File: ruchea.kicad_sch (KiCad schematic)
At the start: 14 parts, among them J10 Conn_01x04, J11 Conn_01x04, J12 Conn_01x04, J14 Conn_01x03, J2 Conn_01x04, J3 Conn_01x03, J4 Conn_01x04, J5 Conn_01x04, J6 Conn_01x02, J7 Conn_01x02, J8 Conn_01x03, J9 Conn_01x03

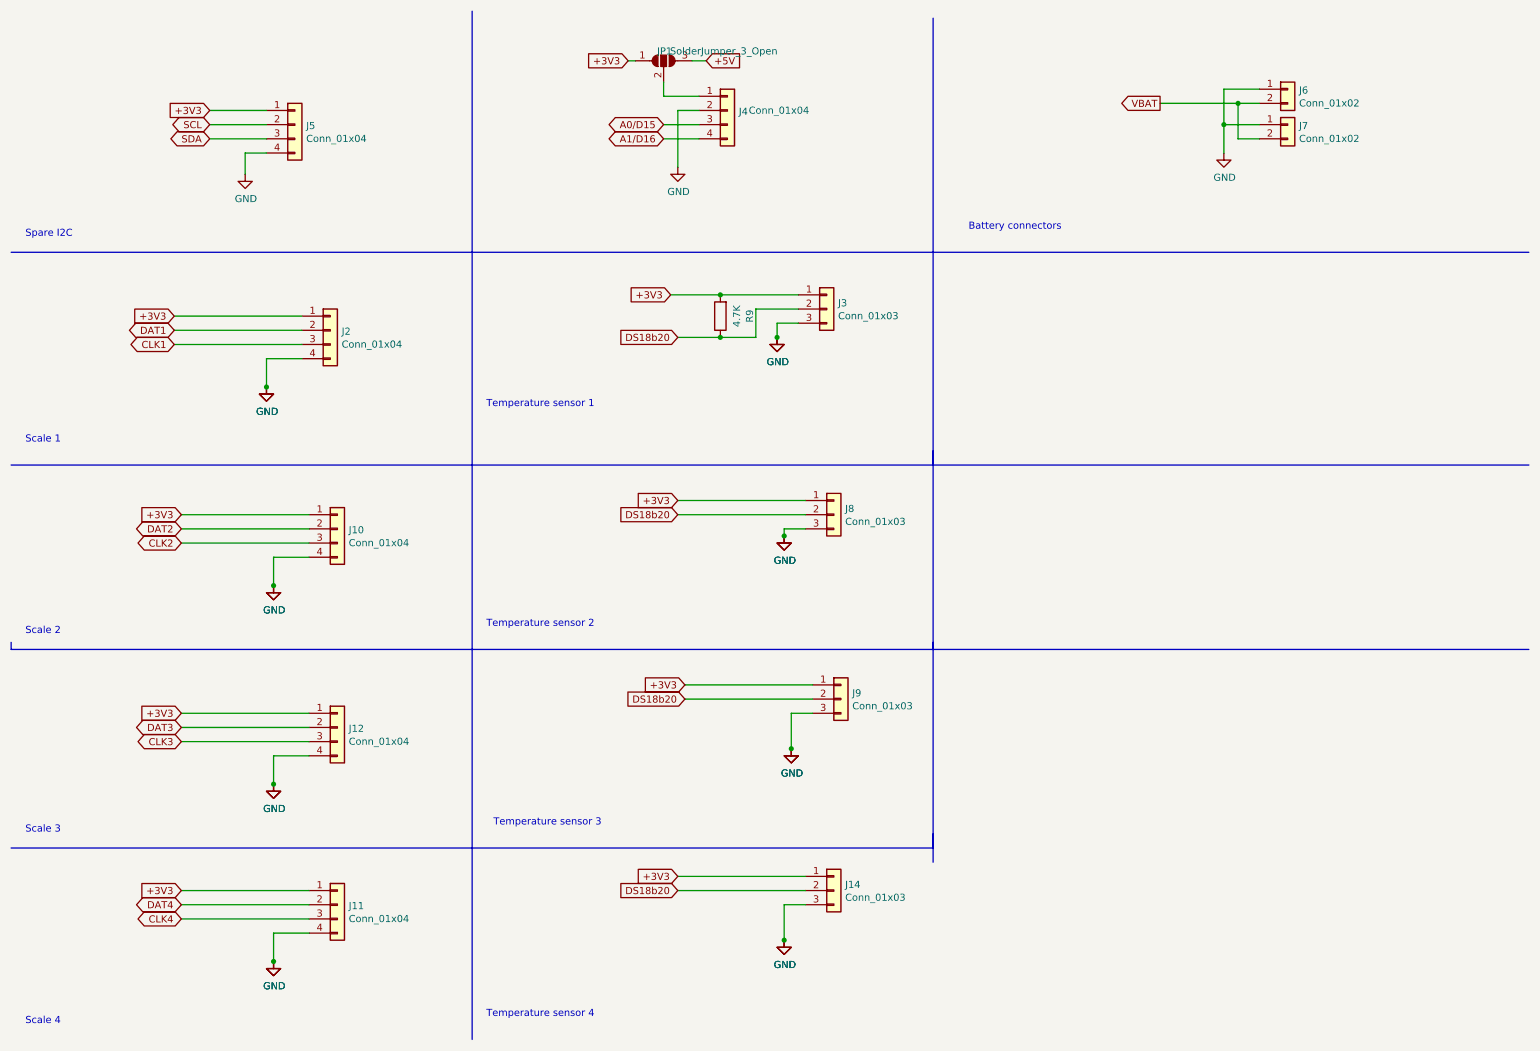
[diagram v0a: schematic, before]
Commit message: Added HX711
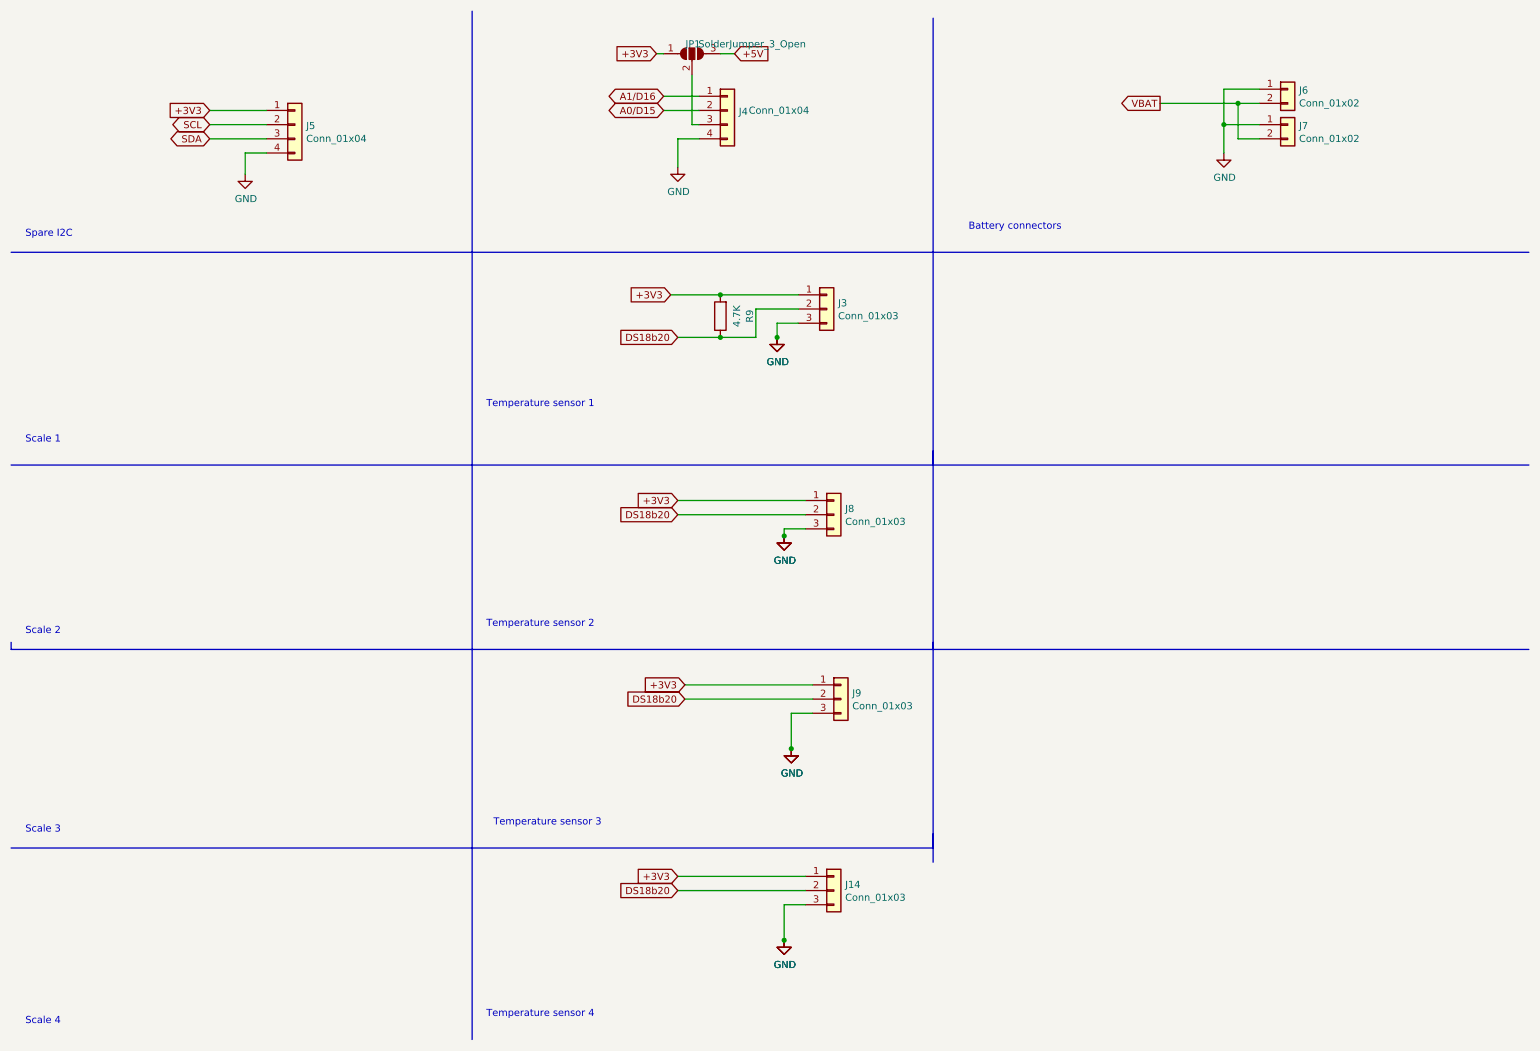
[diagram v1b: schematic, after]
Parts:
- removed J10, J11, J12, J2: Conn_01x04, Connector_JST:JST_PH_B4B-PH-K_1x04_P2.00mm_Vertical, symbol Connector_Generic:Conn_01x04
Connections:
- net A0/D15: now also J4.2 (Pin_2); no longer J4.3 (Pin_3)
- net A1/D16: now also J4.1 (Pin_1); no longer J4.4 (Pin_4)
- net GND: now also J4.4 (Pin_4); no longer J4.2 (Pin_2)
- net at JP1.2 (C): now also J4.3 (Pin_3); no longer J4.1 (Pin_1)
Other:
- moved on the sheet: JP1

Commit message: update
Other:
- note removed: "Scale 1"
- note removed: "Scale 2"
- note removed: "Scale 3"
- note removed: "Scale 4"
- moved on the sheet: J14, J3, J4, J8, J9, JP1, R9

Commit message: Update
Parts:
- removed J4: Conn_01x04, Connector_JST:JST_PH_B4B-PH-K_1x04_P2.00mm_Vertical, symbol Connector_Generic:Conn_01x04
- added C50: 0.1µF, Capacitor_SMD:C_0603_1608Metric, symbol Device:C
- added J11, J12, J17, J18: Conn_01x04, Connector_JST:JST_PH_B4B-PH-K_1x04_P2.00mm_Vertical, symbol Connector_Generic:Conn_01x04
- added J4: Conn_01x03, Connector_JST:JST_PH_B3B-PH-K_1x03_P2.00mm_Vertical, symbol Connector_Generic:Conn_01x03
- added R32, R33, R34, R35, R36, R37, R38, R39, R40: 10K, Resistor_SMD:R_0603_1608Metric, symbol Device:R
- added U4: TCA9548APWR, Package_SO:TSSOP-24_4.4x7.8mm_P0.65mm, symbol Interface_Expansion:TCA9548APWR
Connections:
- net +3V3: no longer J14.1 (Pin_1), J3.1 (Pin_1), J5.1 (Pin_1), J8.1 (Pin_1), J9.1 (Pin_1), R9.2
- net A0/D15: now also J4.1 (Pin_1)
- net GND: now also C50.2, J11.4 (Pin_4), J12.4 (Pin_4), J17.4 (Pin_4), J18.4 (Pin_4), J4.3 (Pin_3), U4.1 (A0), U4.12 (GND), U4.2 (A1), U4.21 (A2)
- net SCL: now also U4.22 (SCL)
- net SDA: now also U4.23 (SDA)
- net at JP1.2 (C): now also J4.2 (Pin_2)
- new net: R32.1, U4.3 (~{RESET})
- new net SC0: J11.1 (Pin_1), R33.1, U4.5 (SC0)
- new net SC1: J17.1 (Pin_1), R35.1, U4.7 (SC1)
- new net SC2: J18.1 (Pin_1), R37.1, U4.9 (SC2)
- new net SC3: J12.1 (Pin_1), R39.1, U4.11 (SC3)
- new net SD0: J11.2 (Pin_2), R34.1, U4.4 (SD0)
- new net SD1: J17.2 (Pin_2), R36.1, U4.6 (SD1)
- new net SD2: J18.2 (Pin_2), R38.1, U4.8 (SD2)
- new net SD3: J12.2 (Pin_2), R40.1, U4.10 (SD3)
- new net VCC: C50.1, J11.3 (Pin_3), J12.3 (Pin_3), J14.1 (Pin_1), J17.3 (Pin_3), J18.3 (Pin_3), J3.1 (Pin_1), J5.1 (Pin_1), J8.1 (Pin_1), J9.1 (Pin_1), R32.2, R33.2, R34.2, R35.2, R36.2, R37.2, R38.2, R39.2, R40.2, R9.2, U4.24 (VCC)
